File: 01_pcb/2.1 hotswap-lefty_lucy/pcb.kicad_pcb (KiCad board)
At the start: 2 copper layers, 251.2 x 81.3 mm, 132 parts, among them J1 TYPE-C-31-M12_13, J2 AVR-ISP-6_mod, J3 Conn_01x01, J4 Conn_01x01, J5 Conn_01x01, J6 Conn_01x01, J7 Conn_01x01, J8 4PIN, K1 KEYSW, K10 KEYSW, K12 KEYSW, K13 KEYSW, K14 KEYSW, K15 KEYSW, K16 KEYSW, K17 KEYSW, K18 KEYSW, K19 KEYSW, K2 KEYSW, K20 KEYSW, K21 KEYSW, K23 KEYSW, K24 KEYSW, K25 KEYSW, K26 KEYSW, K27 KEYSW, K28 KEYSW, K29 KEYSW, K3 KEYSW, K30 KEYSW, K31 KEYSW, K32 KEYSW, K33 KEYSW, K34 KEYSW, K36 KEYSW, K37 KEYSW, K38 KEYSW, K39 KEYSW, K4 KEYSW, K42 KEYSW, K43 KEYSW, K44 KEYSW, K45 KEYSW, K46 KEYSW, K47 KEYSW, K48 KEYSW, K49 KEYSW, K5 KEYSW, K50 KEYSW, K51 KEYSW, K52 KEYSW, K6 KEYSW, K7 KEYSW, K8 KEYSW, K9 KEYSW, SW1 SW_PUSH, U1 ATMEGA32U4, U2 PRTR5V0U2X, Y1 16MHz

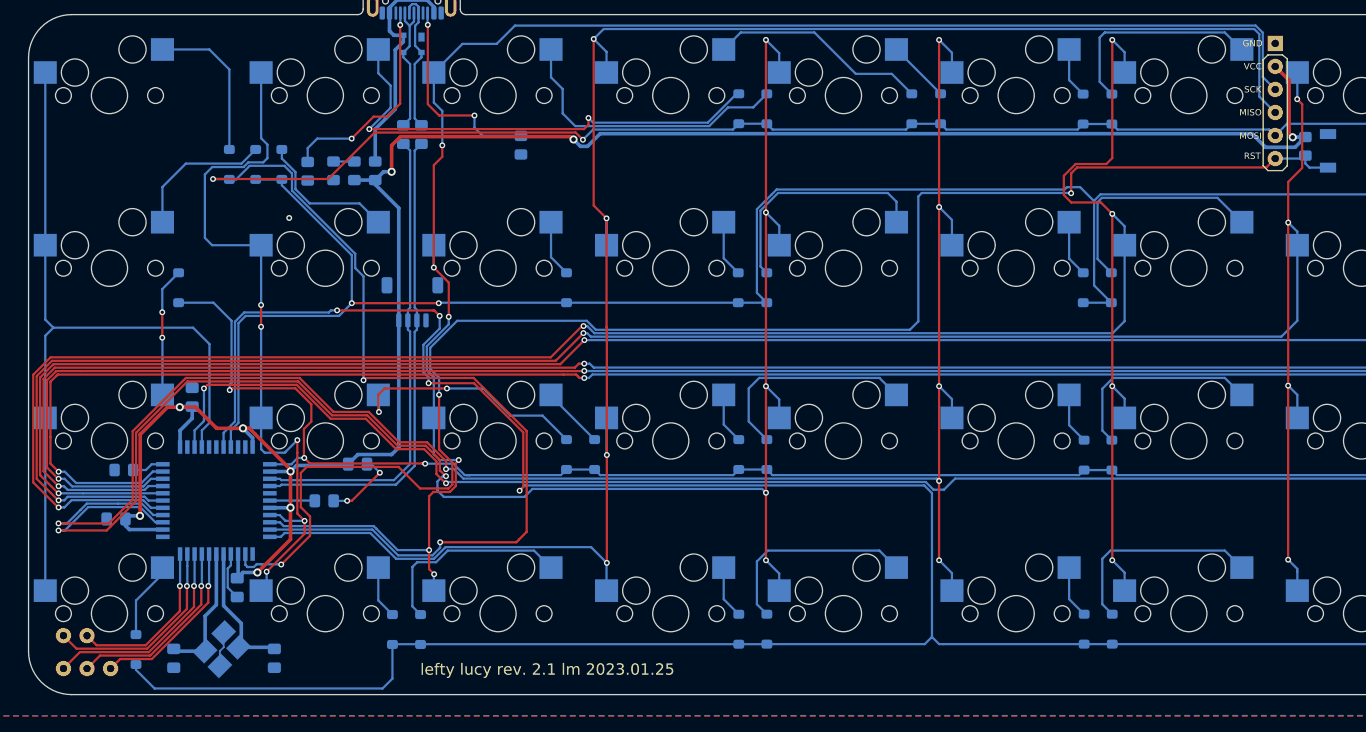
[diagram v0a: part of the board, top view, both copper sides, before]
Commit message: add 3d models to kicad footprints
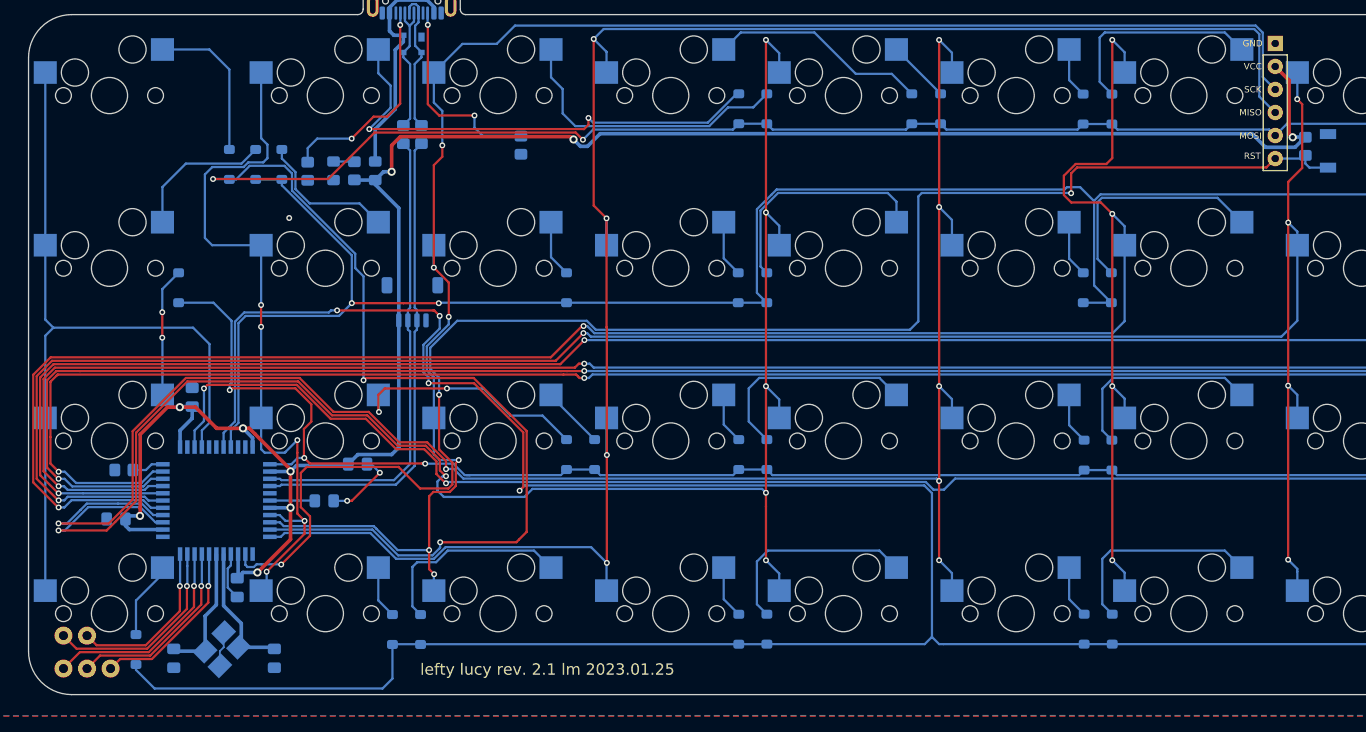
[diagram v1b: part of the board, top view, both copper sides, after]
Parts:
- R1, R2, R3, R4, RCC1, RCC2, RSW1: footprint Resistor_SMD:R_0805_2012Metric_Pad1.15x1.40mm_HandSolder -> Keeb_footprints:R_0805_2012Metric_Pad1.20x1.40mm_HandSolder
